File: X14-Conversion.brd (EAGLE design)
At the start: 50.8 x 68.6 mm, 25 parts, among them P1 282837-2, P2 282837-2, P3 282837-2, U1 BUCK,LM2678S-ADJ

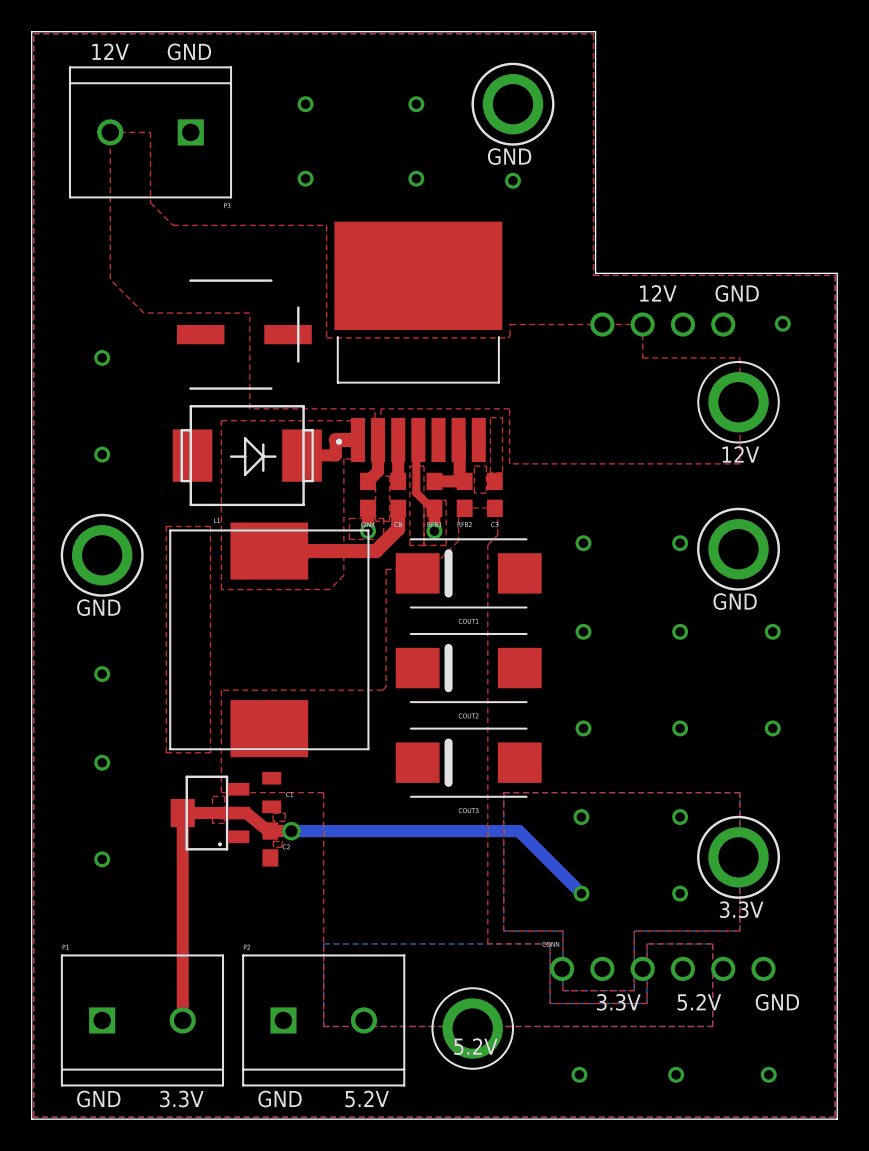
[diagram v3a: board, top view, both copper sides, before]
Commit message: added silkscreen
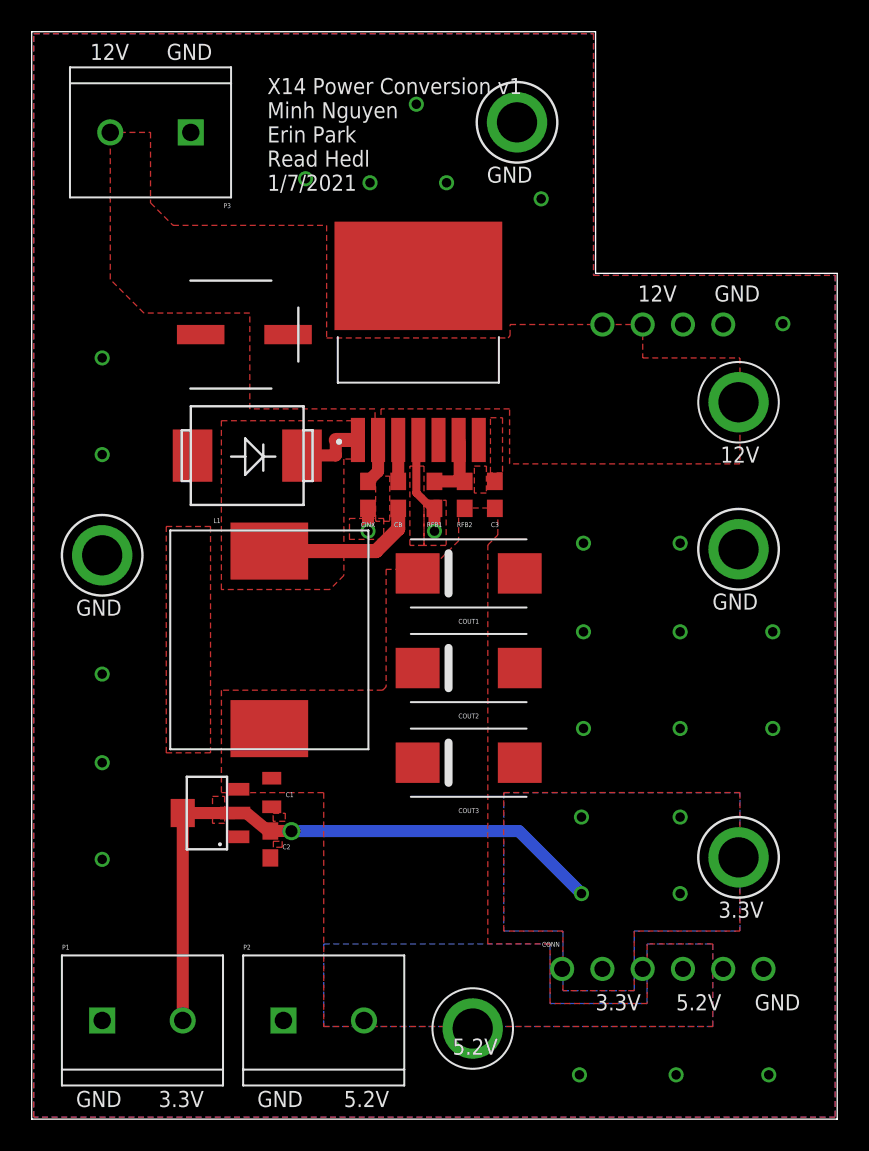
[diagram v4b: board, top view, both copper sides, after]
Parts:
- moved U$5 1.17 mm to (30.6, 62.9)
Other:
- board text added: "X14 Power Conversion v1 Minh Nguyen Erin Park Read Hedl 1/7/2021"
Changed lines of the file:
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@@
 <?xml version="1.0" encoding="utf-8"?>
 <!DOCTYPE eagle SYSTEM "eagle.dtd">
-<eagle version="9.6.2">
+<eagle version="9.5.0">
 <drawing>
 <settings>
@@
 <text x="42.926" y="32.131" size="1.016" layer="21">GND</text>
 <text x="2.794" y="31.75" size="1.016" layer="21">GND</text>
-<text x="28.702" y="60.198" size="1.016" layer="21">GND</text>
+<text x="28.702" y="59.055" size="1.016" layer="21">GND</text>
 <text x="35.56" y="6.858" size="1.016" layer="21">3.3V</text>
 <text x="40.64" y="6.858" size="1.016" layer="21">5.2V</text>
@@
 <text x="38.227" y="51.562" size="1.016" layer="21">12V</text>
 <text x="43.053" y="51.562" size="1.016" layer="21">GND</text>
+<text x="14.859" y="58.547" size="1.016" layer="25">X14 Power Conversion v1
+Minh Nguyen
+Erin Park
+Read Hedl
+1/7/2021
+</text>
 </plain>
 <attributes>
@@
 </class>
 </classes>
-<designrules name="477">
+<designrules name="ECE_Senior_Design">
 <description language="de">&lt;b&gt;EAGLE Design Rules&lt;/b&gt;
 &lt;p&gt;
@@
 Einstellungen hier und speichern die Design Rules unter
 einem neuen Namen ab.</description>
-<description language="en">description[de] = &lt;b&gt;EAGLE Design Rules&lt;/b&gt;
-&lt;p&gt;
-Die Standard-Design-Rules sind so gewÃ¤hlt, dass sie fÃ¼r
-die meisten Anwendungen passen. Sollte ihre Platine
-besondere Anforderungen haben, treffen Sie die erforderlichen
-Einstellungen hier und speichern die Design Rules unter
-einem neuen Namen ab.
-description[en] = &lt;b&gt;ECE 402/477 Design Rules Version 2&lt;/b&gt;
+<description language="en">&lt;b&gt;ECE 402/477 Design Rules Version 2&lt;/b&gt;
 &lt;p&gt;
 These are the design rules to use for Purdue University electrical and computer engineering senior design PCBs.
@@
 Please make sure your boards conform to these design rules.
 &lt;/p&gt;
-layerSetup = (1*16)
-mtCopper = 0.0356mm 0.0356mm 0.0356mm 0.0356mm 0.0356mm 0.0356mm 0.0356mm 0.0356mm 0.0356mm 0.0356mm 0.0356mm 0.0356mm 0.0356mm 0.0356mm 0.0356mm 0.0356mm
-mtIsolate = 1.5011mm 0.1499mm 0.2007mm 0.1499mm 0.2007mm 0.1499mm 0.2007mm 0.1499mm 0.2007mm 0.1499mm 0.2007mm 0.1499mm 0.2007mm 0.1499mm 0.2007mm
-mdWireWire = 8mil
-mdWirePad = 8mil
-mdWireVia = 8mil
-mdPadPad = 6mil
-mdPadVia = 8mil
-mdViaVia = 8mil
-mdSmdPad = 6mil
-mdSmdVia = 6mil
-mdSmdSmd = 6mil
-mdViaViaSameLayer = 8mil
-mnLayersViaInSmd = 2
-mdCopperDimension = 15mil
-mdDrill = 8mil
-mdSmdStop = 0mil
-msWidth = 8mil
-msDrill = 13mil
-msMicroVia = 13mil
-msBlindViaRatio = 0.500000
-rvPadTop = 0.250000
-rvPadInner = 0.250000
-rvPadBottom = 0.250000
-rvViaOuter = 0.250000
-rvViaInner = 0.250000
-rvMicroViaOuter = 0.250000
-rvMicroViaInner = 0.250000
-rlMinPadTop = 7mil
-rlMaxPadTop = 20mil
-rlMinPadInner = 7mil
-rlMaxPadInner = 20mil
-rlMinPadBottom = 7mil
-rlMaxPadBottom = 20mil
-rlMinViaOuter = 7mil
-rlMaxViaOuter = 20mil
-rlMinViaInner = 7mil
-rlMaxViaInner = 20mil
-rlMinMicroViaOuter = 4mil
-rlMaxMicroViaOuter = 20mil
-rlMinMicroViaInner = 4mil
-rlMaxMicroViaInner = 20mil
-psTop = -1
-psBottom = -1
-psFirst = -1
-psElongationLong = 100
-psElongationOffset = 100
-mvStopFrame = 1.000000
-mvCreamFrame = 0.000000
-mlMinStopFrame = 3mil
-mlMaxStopFrame = 3mil
-mlMinCreamFrame = 0mil
-mlMaxCreamFrame = 0mil
-mlViaStopLimit = 0mil
-srRoundness = 0.000000
-srMinRoundness = 0mil
-srMaxRoundness = 0mil
-slThermalIsolate = 10mil
-slThermalsForVias = 0
-dpMaxLengthDifference = 10mm
-dpGapFactor = 2.500000
-checkGrid = 0
-checkAngle = 0
-checkFont = 1
-checkRestrict = 1
-useDiameter = 13
-maxErrors = 50
 </description>
 <param name="layerSetup" value="(1*16)"/>
-<param name="mtCopper" value="0.035mm 0.035mm 0.035mm 0.035mm 0.035mm 0.035mm 0.035mm 0.035mm 0.035mm 0.035mm 0.035mm 0.035mm 0.035mm 0.035mm 0.035mm 0.035mm"/>
-<param name="mtIsolate" value="1.5mm 0.15mm 0.2mm 0.15mm 0.2mm 0.15mm 0.2mm 0.15mm 0.2mm 0.15mm 0.2mm 0.15mm 0.2mm 0.15mm 0.2mm"/>
-<param name="mdWireWire" value="6mil"/>
-<param name="mdWirePad" value="6mil"/>
-<param name="mdWireVia" value="6mil"/>
+<param name="mtCopper" value="0.0356mm 0.0356mm 0.0356mm 0.0356mm 0.0356mm 0.0356mm 0.0356mm 0.0356mm 0.0356mm 0.0356mm 0.0356mm 0.0356mm 0.0356mm 0.0356mm 0.0356mm 0.0356mm"/>
+<param name="mtIsolate" value="1.5011mm 0.1499mm 0.2007mm 0.1499mm 0.2007mm 0.1499mm 0.2007mm 0.1499mm 0.2007mm 0.1499mm 0.2007mm 0.1499mm 0.2007mm 0.1499mm 0.2007mm"/>
+<param name="mdWireWire" value="8mil"/>
+<param name="mdWirePad" value="8mil"/>
+<param name="mdWireVia" value="8mil"/>
 <param name="mdPadPad" value="6mil"/>
-<param name="mdPadVia" value="6mil"/>
-<param name="mdViaVia" value="6mil"/>
+<param name="mdPadVia" value="8mil"/>
+<param name="mdViaVia" value="8mil"/>
 <param name="mdSmdPad" value="6mil"/>
 <param name="mdSmdVia" value="6mil"/>
 <param name="mdSmdSmd" value="6mil"/>
-<param name="mdViaViaSameLayer" value="6mil"/>
+<param name="mdViaViaSameLayer" value="8mil"/>
 <param name="mnLayersViaInSmd" value="2"/>
-<param name="mdCopperDimension" value="40mil"/>
-<param name="mdDrill" value="6mil"/>
+<param name="mdCopperDimension" value="15mil"/>
+<param name="mdDrill" value="8mil"/>
 <param name="mdSmdStop" value="0mil"/>
-<param name="msWidth" value="6mil"/>
-<param name="msDrill" value="0.35mm"/>
-<param name="msMicroVia" value="9.99mm"/>
+<param name="msWidth" value="8mil"/>
+<param name="msDrill" value="13mil"/>
+<param name="msMicroVia" value="13mil"/>
 <param name="msBlindViaRatio" value="0.5"/>
 <param name="rvPadTop" value="0.25"/>
@@
 <param name="rvMicroViaOuter" value="0.25"/>
 <param name="rvMicroViaInner" value="0.25"/>
-<param name="rlMinPadTop" value="10mil"/>
+<param name="rlMinPadTop" value="7mil"/>
 <param name="rlMaxPadTop" value="20mil"/>
-<param name="rlMinPadInner" value="10mil"/>
+<param name="rlMinPadInner" value="7mil"/>
 <param name="rlMaxPadInner" value="20mil"/>
-<param name="rlMinPadBottom" value="10mil"/>
+<param name="rlMinPadBottom" value="7mil"/>
 <param name="rlMaxPadBottom" value="20mil"/>
-<param name="rlMinViaOuter" value="8mil"/>
+<param name="rlMinViaOuter" value="7mil"/>
 <param name="rlMaxViaOuter" value="20mil"/>
-<param name="rlMinViaInner" value="8mil"/>
+<param name="rlMinViaInner" value="7mil"/>
 <param name="rlMaxViaInner" value="20mil"/>
 <param name="rlMinMicroViaOuter" value="4mil"/>
@@
 <param name="mvStopFrame" value="1"/>
 <param name="mvCreamFrame" value="0"/>
-<param name="mlMinStopFrame" value="4mil"/>
-<param name="mlMaxStopFrame" value="4mil"/>
+<param name="mlMinStopFrame" value="3mil"/>
+<param name="mlMaxStopFrame" value="3mil"/>
 <param name="mlMinCreamFrame" value="0mil"/>
 <param name="mlMaxCreamFrame" value="0mil"/>
@@
 <element name="U$3" library="testpoints" package="5.2V_TESTPOINT" value="5.2V_TESTPOINT" x="27.813" y="5.715" smashed="yes"/>
 <element name="U$4" library="testpoints" package="12V_TESTPOINT" value="12V_TESTPOINT" x="44.577" y="45.212" smashed="yes"/>
-<element name="U$5" library="testpoints" package="GND_TESTPOINT" value="GND_TESTPOINT" x="30.353" y="64.008" smashed="yes"/>
+<element name="U$5" library="testpoints" package="GND_TESTPOINT" value="GND_TESTPOINT" x="30.607" y="62.865" smashed="yes"/>
 <element name="U$6" library="testpoints" package="GND_TESTPOINT" value="GND_TESTPOINT" x="4.445" y="35.56" smashed="yes"/>
 <element name="U$7" library="testpoints" package="GND_TESTPOINT" value="GND_TESTPOINT" x="44.577" y="35.941" smashed="yes"/>
@@
 <via x="40.894" y="30.734" extent="1-16" drill="0.6"/>
 <via x="46.736" y="30.734" extent="1-16" drill="0.6"/>
-<via x="17.272" y="64.008" extent="1-16" drill="0.6"/>
+<via x="21.336" y="59.055" extent="1-16" drill="0.6"/>
 <via x="17.272" y="59.309" extent="1-16" drill="0.6"/>
-<via x="24.257" y="59.309" extent="1-16" drill="0.6"/>
+<via x="26.162" y="59.055" extent="1-16" drill="0.6"/>
 <via x="24.257" y="64.008" extent="1-16" drill="0.6"/>
-<via x="30.353" y="59.182" extent="1-16" drill="0.6"/>
+<via x="32.131" y="58.039" extent="1-16" drill="0.6"/>
 <via x="40.894" y="24.638" extent="1-16" drill="0.6"/>
 <via x="46.736" y="24.638" extent="1-16" drill="0.6"/>
@@
 </drawing>
 <compatibility>
+<note version="6.3" minversion="6.2.2" severity="warning">
+Since Version 6.2.2 text objects can contain more than one line,
+which will not be processed correctly with this version.
+</note>
 <note version="8.2" severity="warning">
 Since Version 8.2, EAGLE supports online libraries. The ids

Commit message: Reduce board size
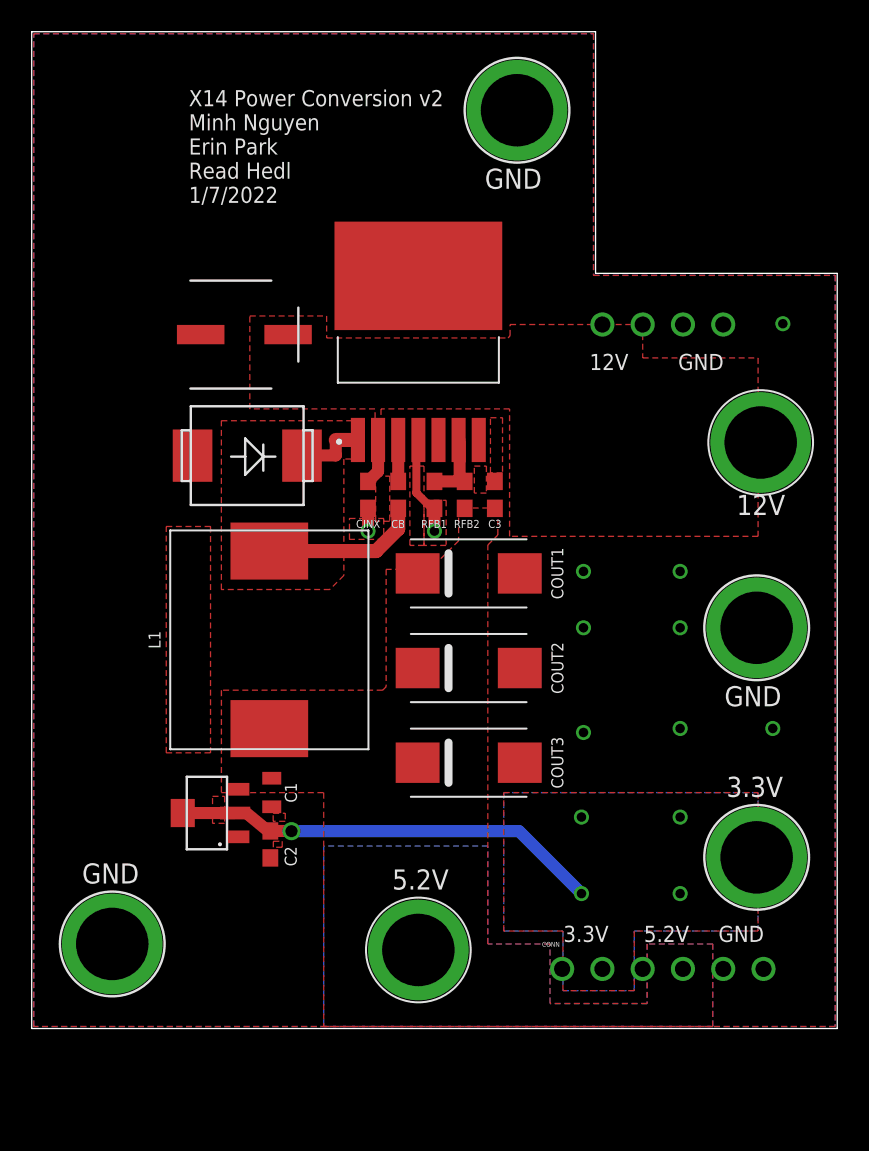
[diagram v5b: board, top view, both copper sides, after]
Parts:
- removed P1, P2, P3: 282837-2, ScrewPoints_282837-2:TE_282837-2
- moved U$6 24.5 mm to (5.08, 11.0)
- moved U$3 6.02 mm to (24.4, 10.7)
- moved U$7 5.08 mm to (45.7, 31.0)
- moved U$4 2.90 mm to (46.0, 42.7)
- moved U$2 1.14 mm to (45.7, 16.5)
- moved U$5 0.76 mm to (30.6, 63.6)
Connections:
- net 12V: no longer P3.2
- net 3.3V: no longer P1.2
- net 5.2V: no longer P2.2
- net GND: no longer P1.1, P2.1, P3.1
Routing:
- net 3.3V: track 40.3 -> 27.2 mm
- net GND: vias 24 -> 10
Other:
- board size 50.8 x 68.6 mm -> 50.8 x 62.9 mm
- board text added: "X14 Power Conversion v2 Minh Nguyen Erin Park Read Hedl 1/7/2022"
- board text removed: "X14 Power Conversion v1 Minh Nguyen Erin Park Read Hedl 1/7/2021"

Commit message: Update X14-Conversion.brd
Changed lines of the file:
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@@
 <wire x1="24.257" y1="42.705" x2="24.257" y2="39.497" width="0.508" layer="1"/>
 <wire x1="24.257" y1="39.497" x2="25.4" y2="38.354" width="0.508" layer="1"/>
-<wire x1="25.4" y1="38.52" x2="29.21" y2="40.22" width="0" layer="19" extent="1-1"/>
 </signal>
 <signal name="3.3V">
@@
 <vertex x="38.5318" y="48.006"/>
 <vertex x="45.8089" y="48.006"/>
-<vertex x="45.8089" y="36.7538"/>
-<vertex x="30.1371" y="36.7538"/>
-<vertex x="30.1371" y="44.7929"/>
+<vertex x="45.8089" y="38.5318"/>
+<vertex x="32.9311" y="38.5318"/>
+<vertex x="32.9311" y="44.7929"/>
 <vertex x="22.02815" y="44.7929"/>
 <vertex x="22.02815" y="41.783"/>
